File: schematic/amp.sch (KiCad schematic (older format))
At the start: 35 parts, among them J2 Conn_01x02, J3 Conn_01x02, Q3 2N3906, Q4 2N3904, Q5 TIP31A, Q6 TIP32A, Q7 2N3055, Q8 2N3055

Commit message: updated a few values based on the final parts used
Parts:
- RV1: value 120k -> 220k
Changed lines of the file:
@@
 P 4200 3400
 F 0 "RV1" H 4130 3354 50  0000 R CNN
-F 1 "120k" H 4130 3445 50  0000 R CNN
+F 1 "220k" H 4130 3445 50  0000 R CNN
 F 2 "Potentiometer_THT:Potentiometer_Piher_PT-6-V_Vertical" H 4200 3400 50  0001 C CNN
 F 3 "~" H 4200 3400 50  0001 C CNN

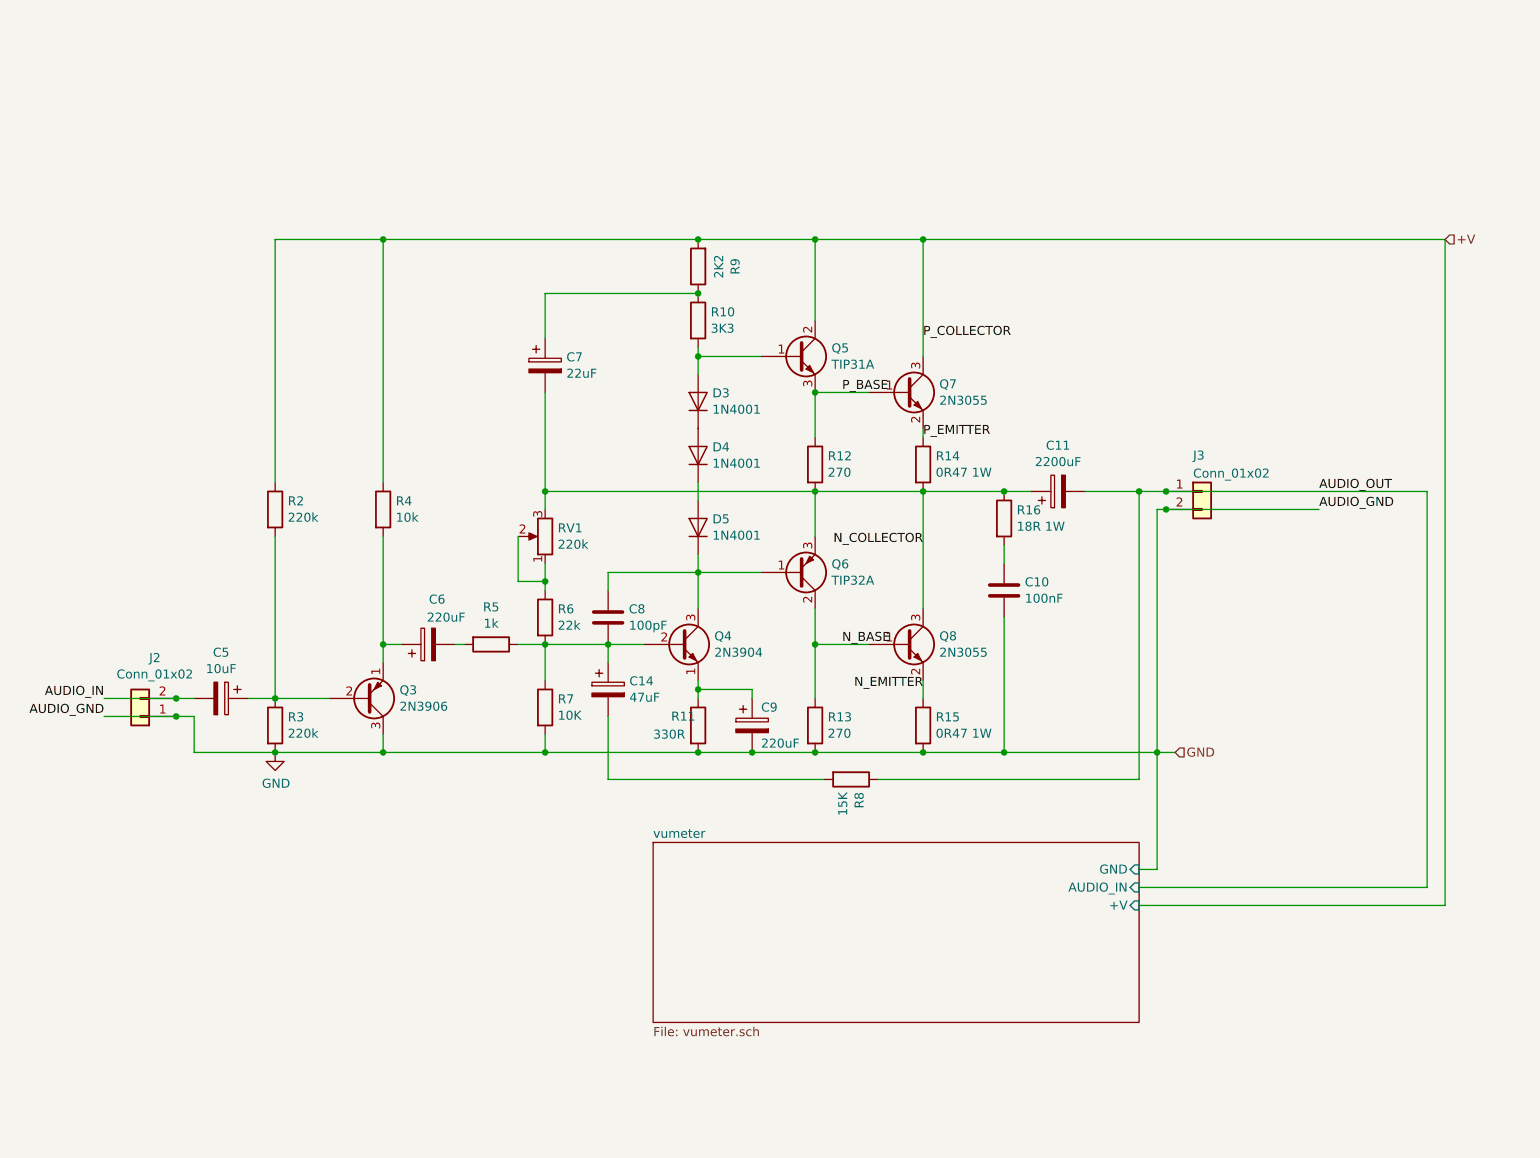
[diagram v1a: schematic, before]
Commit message: first decent version of dual channel opamp version.
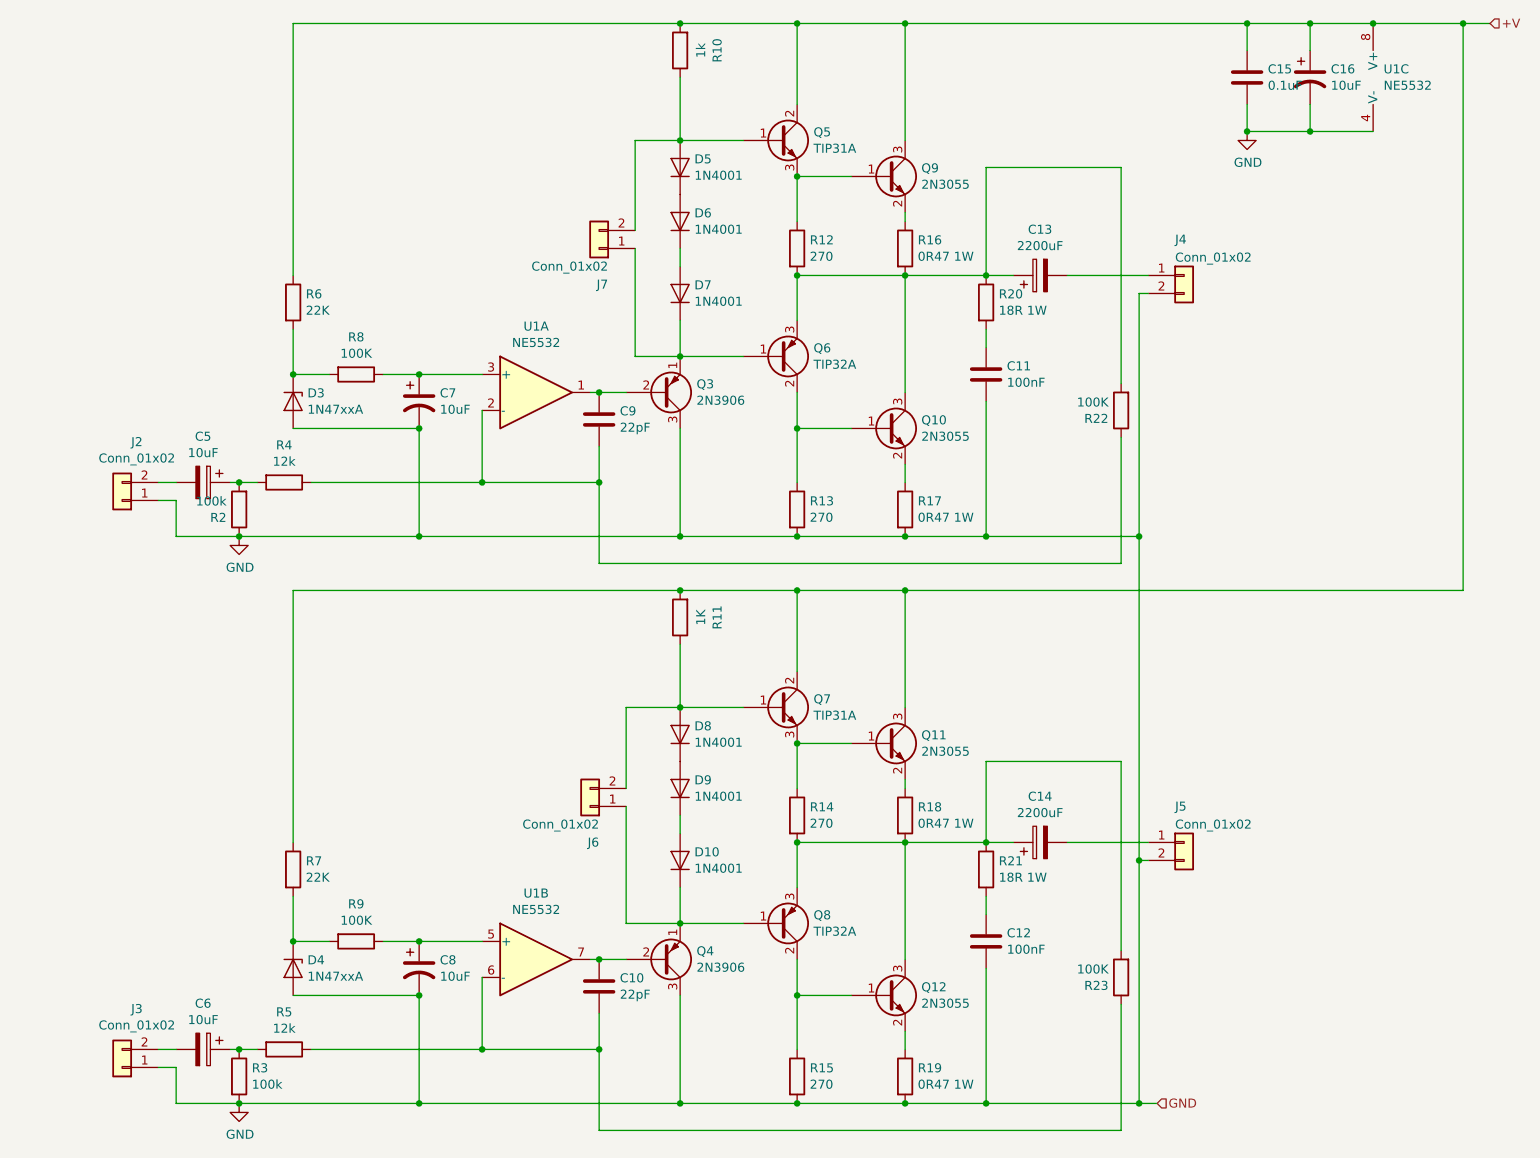
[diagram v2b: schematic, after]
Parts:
- removed C7: 22uF, Capacitor_THT:CP_Radial_D5.0mm_P2.00mm, symbol Device:CP
- removed C8: 100pF, Capacitor_THT:C_Rect_L7.0mm_W4.5mm_P5.00mm, symbol Device:C
- removed C9: 220uF, Capacitor_THT:CP_Radial_D10.0mm_P5.00mm, symbol Device:CP
- removed Q4: 2N3904, Package_TO_SOT_THT:TO-92_Wide, symbol Transistor_BJT:2N3904
- removed R10: 3K3, Resistor_THT:R_Axial_DIN0207_L6.3mm_D2.5mm_P10.16mm_Horizontal, symbol Device:R
- removed RV1: 220k, Potentiometer_THT:Potentiometer_Piher_PT-6-V_Vertical, symbol Device:R_POT
- added C10, C9: 22pF, Capacitor_THT:C_Disc_D4.3mm_W1.9mm_P5.00mm, symbol Device:C
- added C12: 100nF, Capacitor_THT:C_Rect_L7.0mm_W6.0mm_P5.00mm, symbol Device:C
- added C15: 0.1uF, Capacitor_THT:C_Disc_D4.3mm_W1.9mm_P5.00mm, symbol Device:C
- added C16, C7, C8: 10uF, Capacitor_THT:CP_Radial_D5.0mm_P2.00mm, symbol Device:CP1
- added D10, D8, D9: 1N4001, symbol Device:D
- added D3, D4: 1N47xxA, Diode_THT:D_DO-41_SOD81_P10.16mm_Horizontal, symbol Diode:1N47xxA
- added J3: Conn_01x02, Connector_PinHeader_2.54mm:PinHeader_1x02_P2.54mm_Vertical, symbol Connector_Generic:Conn_01x02
- added J5, J6, J7: Conn_01x02, Connector_Molex:Molex_KK-396_A-41791-0002_1x02_P3.96mm_Vertical, symbol Connector_Generic:Conn_01x02
- added Q11, Q12: 2N3055, Connector_Molex:Molex_KK-396_A-41791-0003_1x03_P3.96mm_Vertical, symbol Transistor_BJT:2N3055
- added Q4: 2N3906, Package_TO_SOT_THT:TO-92_Wide, symbol Transistor_BJT:2N3906
- added Q7: TIP31A, Package_TO_SOT_THT:TO-220-3_Vertical, symbol Transistor_BJT:TIP41C
- added Q8: TIP32A, Package_TO_SOT_THT:TO-220-3_Vertical, symbol Transistor_BJT:TIP42C
- added R14, R15: 270, Resistor_THT:R_Axial_DIN0207_L6.3mm_D2.5mm_P10.16mm_Horizontal, symbol Device:R
- added R18, R19: 0R47 1W, Resistor_THT:R_Axial_DIN0617_L17.0mm_D6.0mm_P20.32mm_Horizontal, symbol Device:R
- added R21: 18R 1W, Resistor_THT:R_Axial_DIN0414_L11.9mm_D4.5mm_P15.24mm_Horizontal, symbol Device:R
- added R23, R8, R9: 100K, Resistor_THT:R_Axial_DIN0207_L6.3mm_D2.5mm_P10.16mm_Horizontal, symbol Device:R
- added U1: NE5532, Package_DIP:DIP-8_W7.62mm_LongPads, symbol Amplifier_Operational:NE5532
- C13: renamed from C11; footprint Capacitor_THT:CP_Radial_D18.0mm_P7.50mm -> Capacitor_THT:CP_Radial_D16.0mm_P7.50mm
- C14: value 47uF -> 2200uF; footprint Capacitor_THT:CP_Radial_D5.0mm_P2.00mm -> Capacitor_THT:CP_Radial_D16.0mm_P7.50mm
- C6: value 220uF -> 10uF; footprint Capacitor_THT:CP_Radial_D10.0mm_P5.00mm -> Capacitor_THT:CP_Radial_D5.0mm_P2.00mm
- D5: renamed from D3; footprint Diode_THT:D_DO-41_SOD81_P10.16mm_Horizontal -> (none)
- D6: renamed from D4; footprint Diode_THT:D_DO-41_SOD81_P10.16mm_Horizontal -> (none)
- D7: renamed from D5; footprint Diode_THT:D_DO-41_SOD81_P10.16mm_Horizontal -> (none)
- R10: renamed from R9; value 2K2 -> 1k
- R11: value 330R -> 1K
- R16: renamed from R14; footprint Resistor_THT:R_Axial_Power_L25.0mm_W9.0mm_P27.94mm -> Resistor_THT:R_Axial_DIN0617_L17.0mm_D6.0mm_P20.32mm_Horizontal
- R17: renamed from R15; footprint Resistor_THT:R_Axial_Power_L25.0mm_W9.0mm_P27.94mm -> Resistor_THT:R_Axial_DIN0617_L17.0mm_D6.0mm_P20.32mm_Horizontal
- R2, R3: value 220k -> 100k
- R22: renamed from R8; value 15K -> 100K
- R4: value 10k -> 12k
- R5: value 1k -> 12k
- R6: value 22k -> 22K
- R7: value 10K -> 22K
- renumbered C10 to C11, J3 to J4, Q8 to Q10, Q7 to Q9, R16 to R20
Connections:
- net N_COLLECTOR is gone; now on an unnamed net: C13.1, Q10.3 (C), Q6.3 (E), R12.2, R16.2, R20.1
- net +V: now also R11.2, R6.1, R7.1, C15.1, C16.1, Q11.3 (C), Q7.2 (C), U1.8 (V+); no longer R2.1, R4.1
- net GND: now also R2.1, C12.2, C15.2, C16.2, C7.2, C8.2, D3.2 (A), D4.2 (A), J3.1 (Pin_1), J5.2 (Pin_2), Q4.3 (C), R15.2, R19.2, U1.4 (V-); no longer R11.2, R7.2
- net at C5.1, R2.2: now also R4.2; no longer Q3.2 (B), R3.1
- net at R5.2: now also C6.1, R3.1; no longer C6.2
- net at R10.1: now also D5.2 (A), Q5.1 (B), J7.2 (Pin_2)
- net at R22.2: no longer C14.2
- net at R11.1: now also D8.2 (A), J6.2 (Pin_2), Q7.1 (B)
- net at D7.1 (K), Q6.1 (B): now also Q3.1 (E), J7.1 (Pin_1)
- net AUDIO_IN: no longer names the net of C5.2, J2.2 (Pin_2)
- net AUDIO_OUT: no longer names the net of C13.2, J4.1 (Pin_1)
- net AUDIO_OUT: no longer R22.1
- net N_BASE: no longer names the net of Q10.1 (B), Q6.2 (C), R13.1
- net N_EMITTER: no longer names the net of Q10.2 (E), R17.1
- net P_BASE: no longer names the net of Q5.3 (E), Q9.1 (B), R12.1
- net P_EMITTER: no longer names the net of Q9.2 (E), R16.1
- new net: C9.1, Q3.2 (B), U1.1
- new net: C9.2, R22.1, R4.1, U1.2 (-)
- new net: C7.1, R8.1, U1.3 (+)
- new net: D3.1 (K), R6.2, R8.2
- new net: D10.1 (K), J6.1 (Pin_1), Q4.1 (E), Q8.1 (B)
- new net: Q12.1 (B), Q8.2 (C), R15.1
- new net: Q12.2 (E), R19.1
- new net: C14.1, Q12.3 (C), Q8.3 (E), R14.2, R18.2, R21.1, R23.2
- new net: Q11.1 (B), Q7.3 (E), R14.1
- new net: Q11.2 (E), R18.1
- new net: C12.1, R21.2
- new net: C10.2, R23.1, R5.1, U1.6 (-)
- new net: D8.1 (K), D9.2 (A)
- new net: D10.2 (A), D9.1 (K)
- new net: C14.2, J5.1 (Pin_1)
- new net: C6.2, J3.2 (Pin_2)
- new net: C10.1, Q4.2 (B), U1.7
- new net: C8.1, R9.1, U1.5 (+)
- new net: D4.1 (K), R7.2, R9.2
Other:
- moved on the sheet: C11, C13, C5, D5, D6, D7, J2, J4, Q10, Q3, Q5, Q6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

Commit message: cleanup and remove resistor
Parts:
- removed R2, R3: 100k, Resistor_THT:R_Axial_DIN0207_L6.3mm_D2.5mm_P10.16mm_Horizontal, symbol Device:R
- added D11, D12, D13, D14: 1N4001, Diode_THT:D_DO-41_SOD81_P10.16mm_Horizontal, symbol Device:D
- C10, C9: value 22pF -> 1pF
- R22, R23: value 100K -> 470k
- R4, R5: value 12k -> 47k
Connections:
- net GND: now also D13.2 (A), D14.2 (A); no longer D3.2 (A), D4.2 (A)
- new net: D11.1 (K), D3.2 (A)
- new net: D11.2 (A), D13.1 (K)
- new net: D12.1 (K), D4.2 (A)
- new net: D12.2 (A), D14.1 (K)
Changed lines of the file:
@@
 P 7400 2700
 F 0 "R22" H 7470 2746 50  0000 L CNN
-F 1 "100K" H 7470 2655 50  0000 L CNN
+F 1 "470k" H 7470 2655 50  0000 L CNN
 F 2 "Resistor_THT:R_Axial_DIN0207_L6.3mm_D2.5mm_P10.16mm_Horizontal" V 7330 2700 50  0001 C CNN
 F 3 "~" H 7400 2700 50  0001 C CNN
@@
 	5600 3400 6200 3400
 Wire Wire Line
-	2600 3100 2500 3100
-Wire Wire Line
 	6650 2650 6650 3400
 Connection ~ 6200 3400
@@
 P 2750 3100
 F 0 "R4" V 2543 3100 50  0000 C CNN
-F 1 "12k" V 2634 3100 50  0000 C CNN
+F 1 "47k" V 2634 3100 50  0000 C CNN
 F 2 "Resistor_THT:R_Axial_DIN0207_L6.3mm_D2.5mm_P10.16mm_Horizontal" V 2680 3100 50  0001 C CNN
 F 3 "~" H 2750 3100 50  0001 C CNN
@@
 P 4500 2750
 F 0 "C9" H 4615 2796 50  0000 L CNN
-F 1 "22pF" H 4615 2705 50  0000 L CNN
+F 1 "1pF" H 4615 2705 50  0000 L CNN
 F 2 "Capacitor_THT:C_Disc_D4.3mm_W1.9mm_P5.00mm" H 4538 2600 50  0001 C CNN
 F 3 "~" H 4500 2750 50  0001 C CNN
@@
 P 7400 5850
 F 0 "R23" H 7470 5896 50  0000 L CNN
-F 1 "100K" H 7470 5805 50  0000 L CNN
+F 1 "470k" H 7470 5805 50  0000 L CNN
 F 2 "Resistor_THT:R_Axial_DIN0207_L6.3mm_D2.5mm_P10.16mm_Horizontal" V 7330 5850 50  0001 C CNN
 F 3 "~" H 7400 5850 50  0001 C CNN
@@
 	5600 6550 6200 6550
 Wire Wire Line
-	2600 6250 2500 6250
-Wire Wire Line
 	6650 5800 6650 6550
 Connection ~ 6200 6550
@@
 P 2750 6250
 F 0 "R5" V 2543 6250 50  0000 C CNN
-F 1 "12k" V 2634 6250 50  0000 C CNN
+F 1 "47k" V 2634 6250 50  0000 C CNN
 F 2 "Resistor_THT:R_Axial_DIN0207_L6.3mm_D2.5mm_P10.16mm_Horizontal" V 2680 6250 50  0001 C CNN
 F 3 "~" H 2750 6250 50  0001 C CNN
@@
 P 4500 5900
 F 0 "C10" H 4615 5946 50  0000 L CNN
-F 1 "22pF" H 4615 5855 50  0000 L CNN
+F 1 "1pF" H 4615 5855 50  0000 L CNN
 F 2 "Capacitor_THT:C_Disc_D4.3mm_W1.9mm_P5.00mm" H 4538 5750 50  0001 C CNN
 F 3 "~" H 4500 5900 50  0001 C CNN
@@
 Wire Wire Line
 	3500 6550 4950 6550
-$Comp
-L Device:R R3
-U 1 1 610526A3
-P 2500 6400
-F 0 "R3" H 2570 6446 50  0000 L CNN
-F 1 "100k" H 2570 6355 50  0000 L CNN
-F 2 "Resistor_THT:R_Axial_DIN0207_L6.3mm_D2.5mm_P10.16mm_Horizontal" V 2430 6400 50  0001 C CNN
-F 3 "~" H 2500 6400 50  0001 C CNN
-	1    2500 6400
-	1    0    0    -1
-$EndComp
-Connection ~ 2500 6250
-Wire Wire Line
-	2500 6250 2450 6250
 Connection ~ 2500 6550
 Wire Wire Line
 	2500 6550 2150 6550
-$Comp
-L Device:R R2
-U 1 1 61052CB2
-P 2500 3250
-F 0 "R2" H 2570 3296 50  0000 L CNN
-F 1 "100k" H 2570 3205 50  0000 L CNN
-F 2 "Resistor_THT:R_Axial_DIN0207_L6.3mm_D2.5mm_P10.16mm_Horizontal" V 2430 3250 50  0001 C CNN
-F 3 "~" H 2500 3250 50  0001 C CNN
-	1    2500 3250
-	-1   0    0    1
-$EndComp
 Connection ~ 2500 3400
-Connection ~ 2500 3100
-Wire Wire Line
-	2500 3100 2450 3100
 Wire Wire Line
 	2150 3400 2500 3400
@@
 Wire Wire Line
 	2500 6550 3500 6550
-Connection ~ 3500 2800
-Connection ~ 3500 5950
 Wire Wire Line
 	7100 1950 7550 1950
@@
 Wire Wire Line
 	7400 1350 7400 2550
-Wire Wire Line
-	2800 2800 3500 2800
-Wire Wire Line
-	2800 5950 3500 5950
 $Comp
 L Connector_Generic:Conn_01x02 J7
@@
 Wire Wire Line
 	4650 5550 4950 5550
+Wire Wire Line
+	2450 3100 2600 3100
+Wire Wire Line
+	2450 6250 2600 6250
+$Comp
+L Device:D D11
+U 1 1 610B09DA
+P 3050 2800
+F 0 "D11" V 3096 2721 50  0000 R CNN
+F 1 "1N4001" V 3005 2721 50  0000 R CNN
+F 2 "Diode_THT:D_DO-41_SOD81_P10.16mm_Horizontal" H 3050 2800 50  0001 C CNN
+F 3 "~" H 3050 2800 50  0001 C CNN
+	1    3050 2800
+	1    0    0    -1
+$EndComp
+$Comp
+L Device:D D13
+U 1 1 610B1262
+P 3350 2800
+F 0 "D13" V 3396 2721 50  0000 R CNN
+F 1 "1N4001" V 3305 2721 50  0000 R CNN
+F 2 "Diode_THT:D_DO-41_SOD81_P10.16mm_Horizontal" H 3350 2800 50  0001 C CNN
+F 3 "~" H 3350 2800 50  0001 C CNN
+	1    3350 2800
+	1    0    0    -1
+$EndComp
+Connection ~ 3500 2800
+$Comp
+L Device:D D12
+U 1 1 610B18CA
+P 3050 5950
+F 0 "D12" V 3096 5871 50  0000 R CNN
+F 1 "1N4001" V 3005 5871 50  0000 R CNN
+F 2 "Diode_THT:D_DO-41_SOD81_P10.16mm_Horizontal" H 3050 5950 50  0001 C CNN
+F 3 "~" H 3050 5950 50  0001 C CNN
+	1    3050 5950
+	1    0    0    -1
+$EndComp
+$Comp
+L Device:D D14
+U 1 1 610B2028
+P 3350 5950
+F 0 "D14" V 3396 5871 50  0000 R CNN
+F 1 "1N4001" V 3305 5871 50  0000 R CNN
+F 2 "Diode_THT:D_DO-41_SOD81_P10.16mm_Horizontal" H 3350 5950 50  0001 C CNN
+F 3 "~" H 3350 5950 50  0001 C CNN
+	1    3350 5950
+	1    0    0    -1
+$EndComp
+Connection ~ 3500 5950
+Wire Wire Line
+	2900 2800 2800 2800
+Wire Wire Line
+	2900 5950 2800 5950
 $EndSCHEMATC
